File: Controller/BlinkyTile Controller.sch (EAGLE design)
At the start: 26 parts, among them CON1 USB_MICROSMT+THRUHULE, Q1 CRYSTAL_4PAD2520, U1 MK20D--VFM5, U2 W25Q80BV, U3 74LVC1G17DCK, U4 74LVC1G17DCK, U5 74LVC1G17DCK

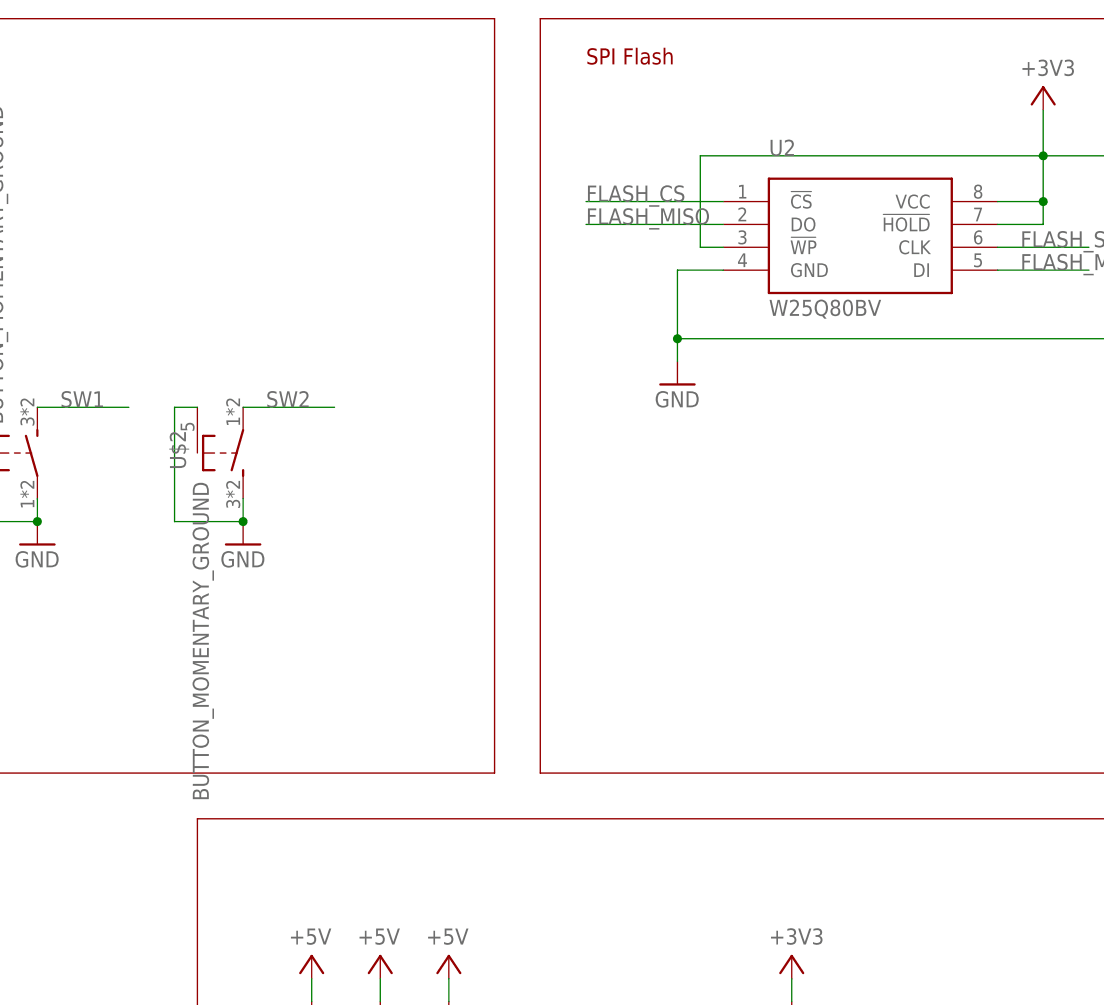
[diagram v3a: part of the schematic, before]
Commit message: Update flash type, add .254mm isolation on top&bottom copper, general cleanup
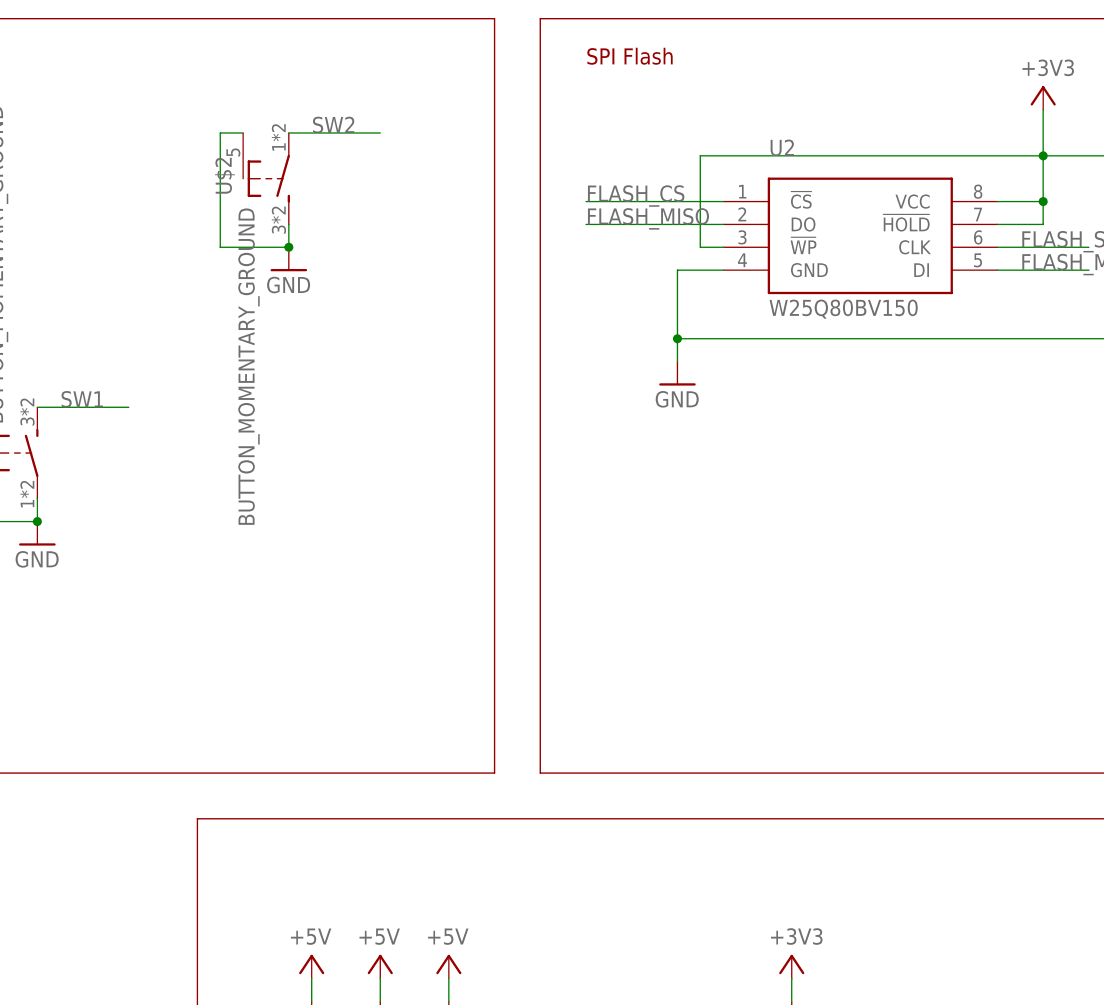
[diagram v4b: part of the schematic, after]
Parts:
- U2: value W25Q80BV -> W25Q80BV150; device Blinkin_Labs:W25Q80BV -> blinkinlabs:W25Q80BV150
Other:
- moved on the sheet: U$2
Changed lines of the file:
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@@
 <part name="GND10" library="SparkFun-Aesthetics" deviceset="GND" device=""/>
 <part name="C5" library="adafruit" deviceset="C-US" device="C0402" value="100nF"/>
-<part name="U2" library="Blinkin_Labs" deviceset="W25Q80BV" device=""/>
+<part name="U2" library="blinkinlabs" deviceset="W25Q80BV" device="150"/>
 <part name="FRAME1" library="frames" deviceset="DINA3_L" device=""/>
 <part name="C1" library="adafruit" deviceset="C-US" device="C0402" value="100nF"/>
@@
 </instance>
 <instance part="L1" gate="G$1" x="53.34" y="195.58" rot="R90"/>
-<instance part="GND2" gate="1" x="261.62" y="190.5"/>
+<instance part="GND2" gate="1" x="266.7" y="220.98"/>
 <instance part="U4" gate="G$1" x="337.82" y="104.14" smashed="yes">
 <attribute name="NAME" x="339.09" y="107.315" size="1.778" layer="95"/>
@@
 <instance part="JP3" gate="G$1" x="180.34" y="190.5" rot="R180"/>
 <instance part="U$1" gate="G$1" x="236.22" y="200.66"/>
-<instance part="U$2" gate="G$1" x="259.08" y="200.66" rot="MR180"/>
+<instance part="U$2" gate="G$1" x="264.16" y="231.14" rot="MR180"/>
 </instances>
 <busses>
@@
 <pinref part="GND2" gate="1" pin="GND"/>
 <pinref part="U$2" gate="G$1" pin="S"/>
-<wire x1="261.62" y1="195.58" x2="261.62" y2="193.04" width="0.1524" layer="91"/>
+<wire x1="266.7" y1="226.06" x2="266.7" y2="223.52" width="0.1524" layer="91"/>
 <pinref part="U$2" gate="G$1" pin="SHIELD"/>
-<wire x1="256.54" y1="205.74" x2="254" y2="205.74" width="0.1524" layer="91"/>
-<wire x1="254" y1="205.74" x2="254" y2="193.04" width="0.1524" layer="91"/>
-<wire x1="254" y1="193.04" x2="261.62" y2="193.04" width="0.1524" layer="91"/>
-<junction x="261.62" y="193.04"/>
+<wire x1="261.62" y1="236.22" x2="259.08" y2="236.22" width="0.1524" layer="91"/>
+<wire x1="259.08" y1="236.22" x2="259.08" y2="223.52" width="0.1524" layer="91"/>
+<wire x1="259.08" y1="223.52" x2="266.7" y2="223.52" width="0.1524" layer="91"/>
+<junction x="266.7" y="223.52"/>
 </segment>
 <segment>
@@
 <net name="SW2" class="0">
 <segment>
-<label x="264.16" y="205.74" size="1.778" layer="95"/>
+<label x="269.24" y="236.22" size="1.778" layer="95"/>
 <pinref part="U$2" gate="G$1" pin="P"/>
-<wire x1="261.62" y1="205.74" x2="271.78" y2="205.74" width="0.1524" layer="91"/>
-</segment>
-<segment>
+<wire x1="266.7" y1="236.22" x2="276.86" y2="236.22" width="0.1524" layer="91"/>
+</segment>
+<segment>

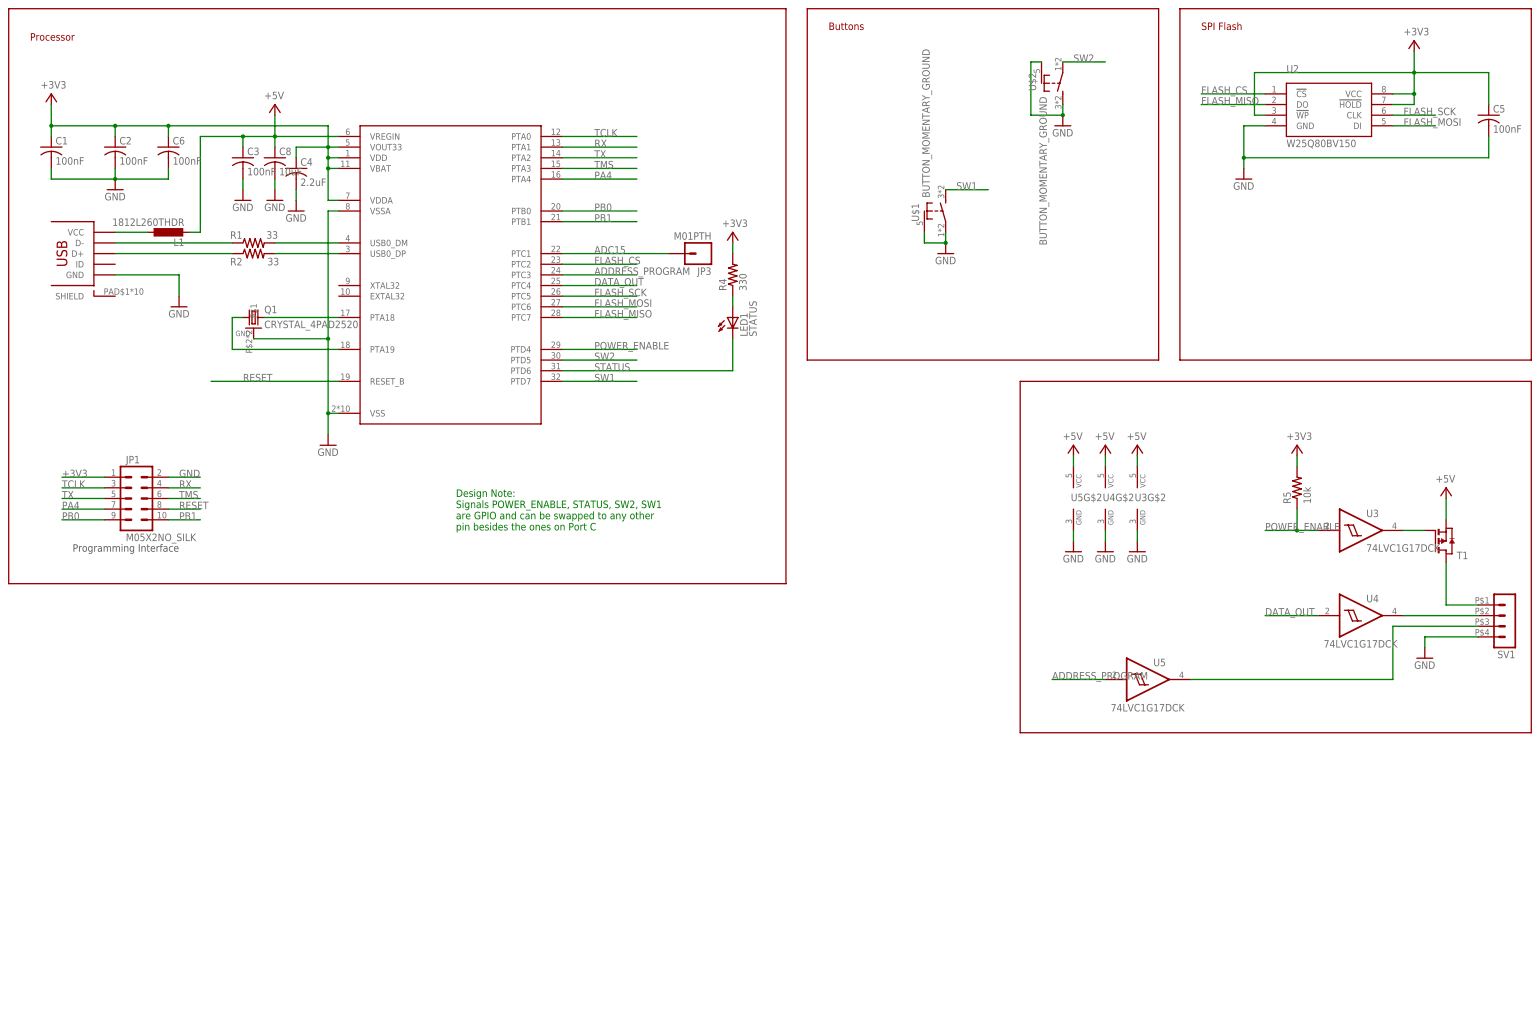
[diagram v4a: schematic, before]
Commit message: Add ferrite beads, move the fuse to the ouput.
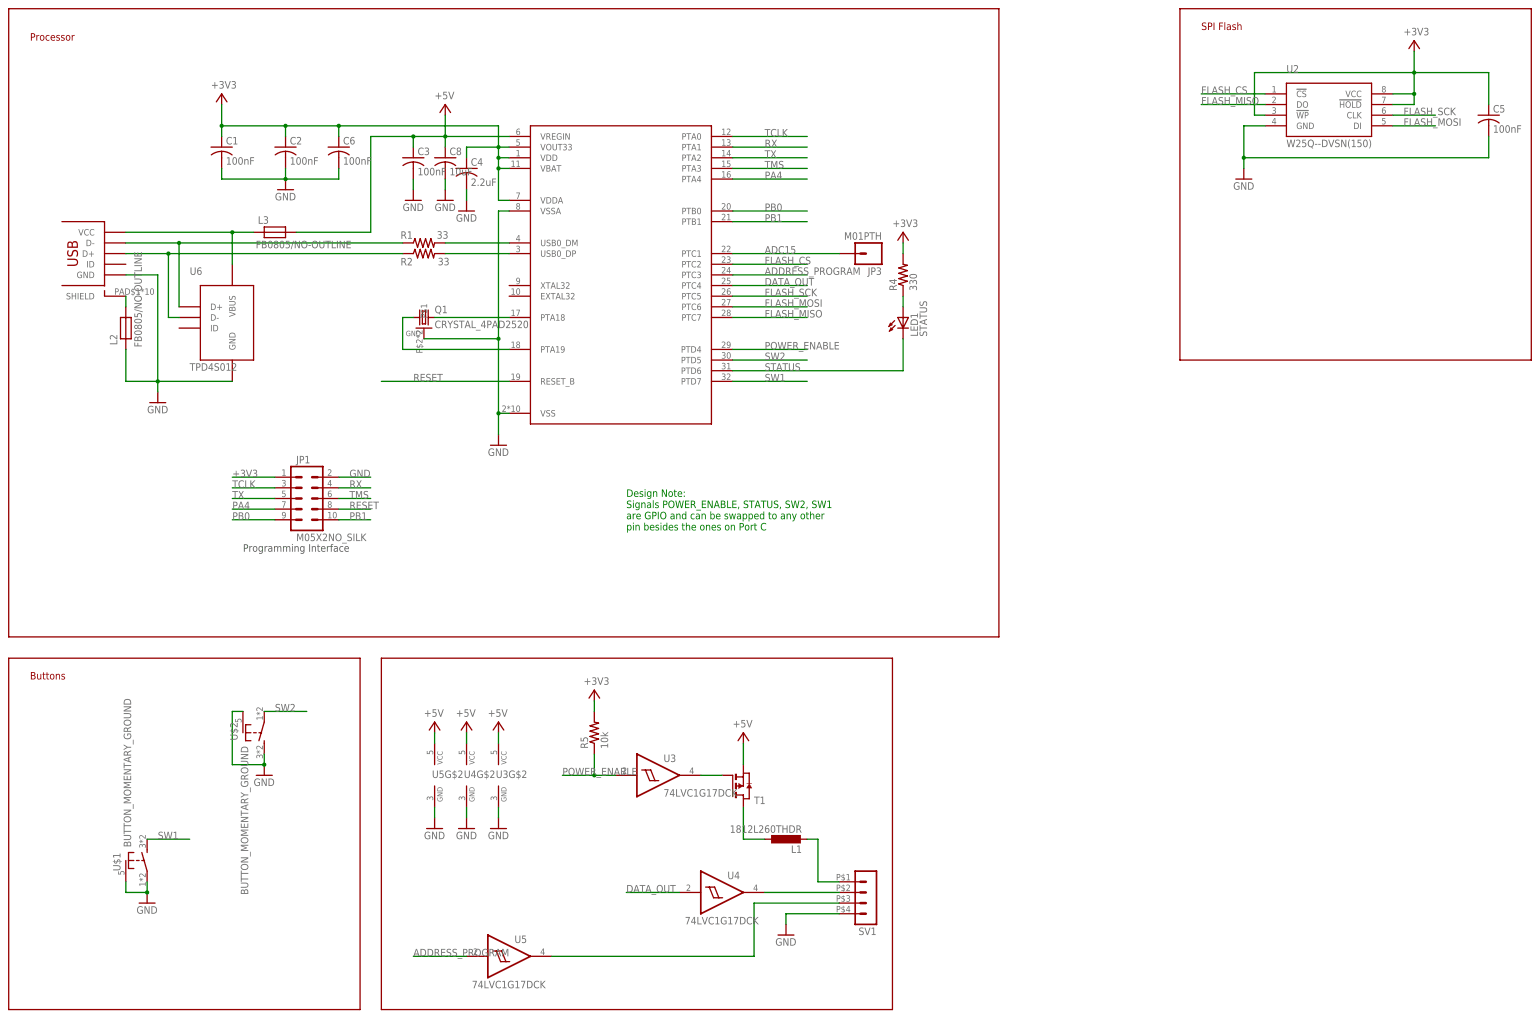
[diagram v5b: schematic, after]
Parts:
- added L2, L3: FB0805/NO-OUTLINE, blinkinlabs:FB0805/NO-OUTLINE
- added U6: TPD4S012, blinkinlabs:TPD4S012
- U2: value W25Q80BV150 -> W25Q--DVSN(150); device blinkinlabs:W25Q80BV150 -> blinkinlabs:W25Q--DVSN(150)
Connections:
- removed net N$9: CON1.D-, R1.1
- new net N$7: CON1.D-, R1.1, U6.D+
- new net N$8: L1.2, SV1.1
- new net SHIELD: CON1.SHIELD, L2.P$1
- net +5V: now also L3.P$1; no longer L1.2
- net GND: now also L2.P$2, U6.GND
- net N$10: now also U6.D-
- net N$3: now also L3.P$2, U6.VBUS; no longer L1.1
- net N$5: now also L1.1; no longer SV1.1
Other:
- moved on the sheet: C1, C2, C3, C4, C6, C8, JP1, JP3, L1, LED1, Q1, R1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

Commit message: Tidy schematic and add values to ferrites, crystal
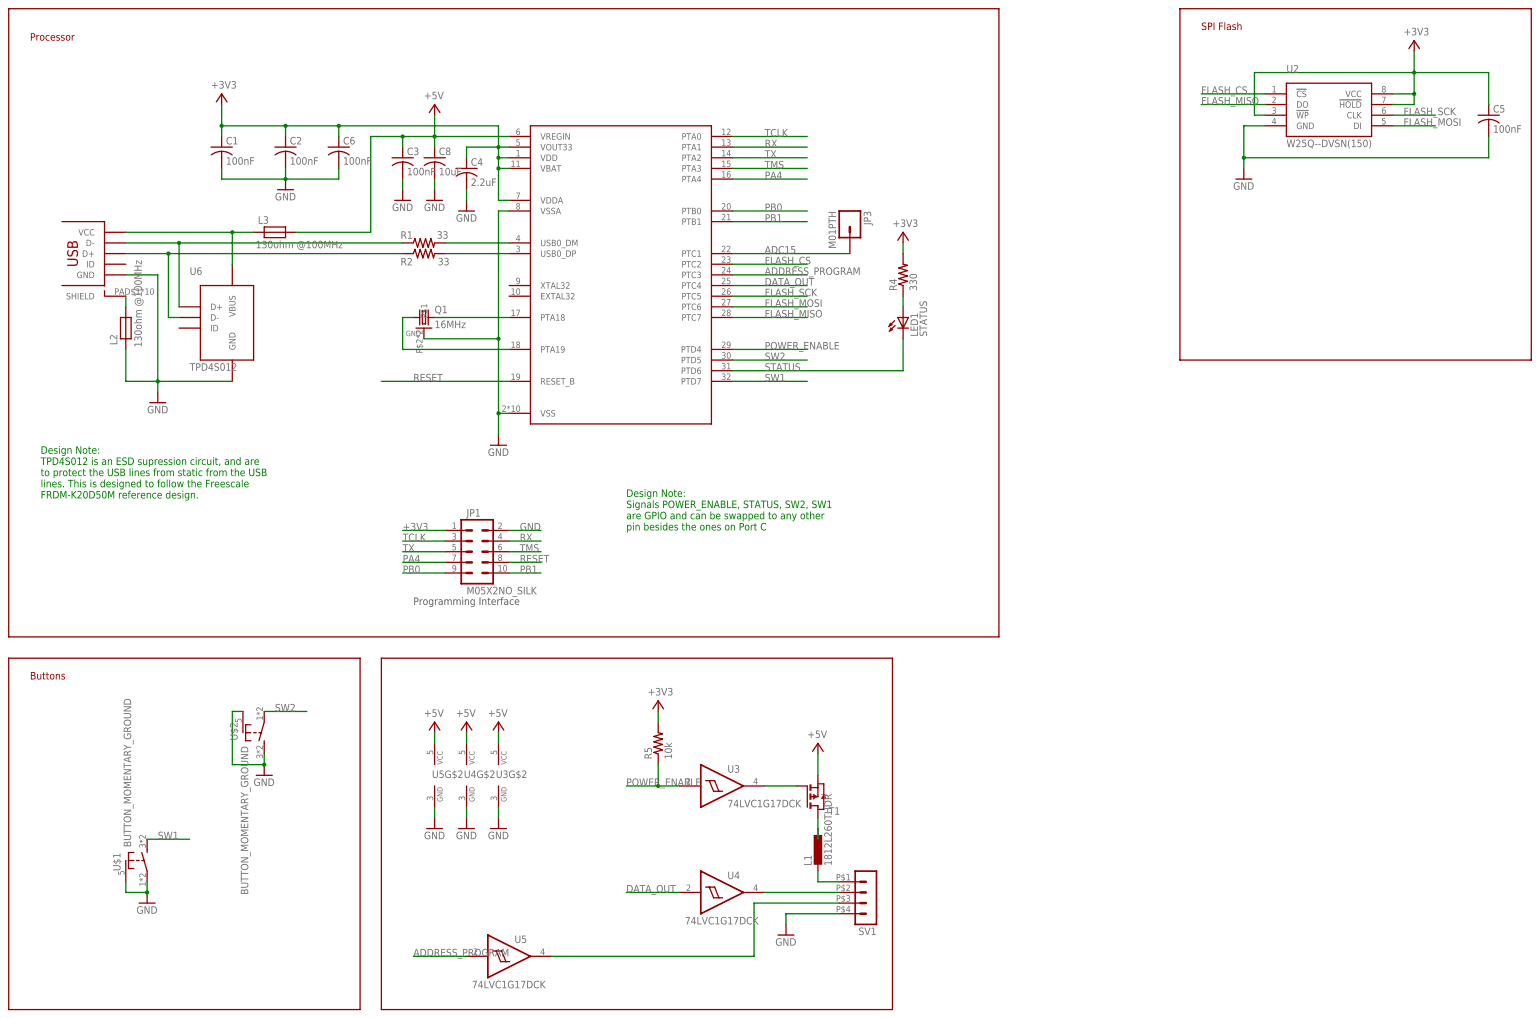
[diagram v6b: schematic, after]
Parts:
- L2, L3: value FB0805/NO-OUTLINE -> 130ohm @100MHz
- Q1: value CRYSTAL_4PAD2520 -> 16MHz
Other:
- note added: "Design Note: TPD4S012 is an ESD supression circuit, and are to protect the USB lines from static from the USB lines. This is designed to follow the Freescale FRDM-K20D50M reference design."
- moved on the sheet: C3, C8, JP1, JP3, L1, R5, T1, U3

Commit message: Controller: Switch back to 208 package for flash chip
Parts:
- U2: value W25Q--DVSN(150) -> W25Q--DVSS(208); device blinkinlabs:W25Q--DVSN(150) -> blinkinlabs:W25Q--DVSS(208)
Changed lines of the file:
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@@
 <part name="GND10" library="SparkFun-Aesthetics" deviceset="GND" device=""/>
 <part name="C5" library="adafruit" deviceset="C-US" device="C0402" value="100nF"/>
-<part name="U2" library="blinkinlabs" deviceset="W25Q--DV" device="SN(150)"/>
+<part name="U2" library="blinkinlabs" deviceset="W25Q--DV" device="SS(208)" value="W25Q--DVSS(208)"/>
 <part name="FRAME1" library="frames" deviceset="DINA3_L" device=""/>
 <part name="C1" library="adafruit" deviceset="C-US" device="C0402" value="100nF"/>
